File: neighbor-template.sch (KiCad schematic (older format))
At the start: 12 parts, among them J1 NEIGHBOR1, J2 NEIGHBOR2, J7 BONUS_ROW

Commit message: copy gsg-kicad-lib footprints to local library remove gsg-kicad-lib dependency
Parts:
- J1, J2: footprint gsg-modules:HEADER-2x20 -> neighbor:HEADER-2x20
- J7: footprint gsg-modules:HEADER-1x20 -> neighbor:HEADER-1x20
- MH1, MH2, MH3, MH4: footprint gsg-modules:HOLE126MIL-COPPER -> neighbor:HOLE126MIL-COPPER
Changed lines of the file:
@@
 LIBS:power
 LIBS:74xx
-LIBS:gsg-symbols
 LIBS:neighbor-template-cache
 EELAYER 29 0
@@
 F 0 "J2" H 15750 3900 50  0000 C CNN
 F 1 "NEIGHBOR2" V 15750 2850 50  0000 C CNN
-F 2 "gsg-modules:HEADER-2x20" H 15700 1900 60  0001 C CNN
+F 2 "neighbor:HEADER-2x20" H 15700 1900 60  0001 C CNN
 F 3 "" H 15700 1900 60  0000 C CNN
 F 4 "Samtec" H 15700 2850 60  0001 C CNN "Manufacturer"
@@
 F 0 "J1" H 15750 6250 50  0000 C CNN
 F 1 "NEIGHBOR1" V 15750 5200 50  0000 C CNN
-F 2 "gsg-modules:HEADER-2x20" H 15700 4250 60  0001 C CNN
+F 2 "neighbor:HEADER-2x20" H 15700 4250 60  0001 C CNN
 F 3 "" H 15700 4250 60  0000 C CNN
 F 4 "Samtec" H 15700 5200 60  0001 C CNN "Manufacturer"
@@
 F 0 "J7" H 15150 8050 50  0000 C CNN
 F 1 "BONUS_ROW" V 15250 7000 50  0000 C CNN
-F 2 "gsg-modules:HEADER-1x20" H 15150 7000 60  0001 C CNN
+F 2 "neighbor:HEADER-1x20" H 15150 7000 60  0001 C CNN
 F 3 "" H 15150 7000 60  0000 C CNN
 F 4 "Samtec" H 15150 7000 60  0001 C CNN "Manufacturer"
@@
 F 0 "MH3" H 13600 950 50  0000 C CNN
 F 1 "MOUNTING_HOLE" V 13750 850 50  0000 C CNN
-F 2 "gsg-modules:HOLE126MIL-COPPER" H 13650 850 60  0001 C CNN
+F 2 "neighbor:HOLE126MIL-COPPER" H 13650 850 60  0001 C CNN
 F 3 "" H 13650 850 60  0000 C CNN
 F 4 "DNP" H 13650 850 60  0001 C CNN "Note"
@@
 F 0 "MH4" H 14100 1100 50  0000 C CNN
 F 1 "MOUNTING_HOLE" V 14250 1000 50  0000 C CNN
-F 2 "gsg-modules:HOLE126MIL-COPPER" H 14150 1000 60  0001 C CNN
+F 2 "neighbor:HOLE126MIL-COPPER" H 14150 1000 60  0001 C CNN
 F 3 "" H 14150 1000 60  0000 C CNN
 F 4 "DNP" H 14150 1000 60  0001 C CNN "Note"
@@
 F 0 "MH1" H 12600 950 50  0000 C CNN
 F 1 "MOUNTING_HOLE" V 12750 850 50  0000 C CNN
-F 2 "gsg-modules:HOLE126MIL-COPPER" H 12650 850 60  0001 C CNN
+F 2 "neighbor:HOLE126MIL-COPPER" H 12650 850 60  0001 C CNN
 F 3 "" H 12650 850 60  0000 C CNN
 F 4 "DNP" H 12650 850 60  0001 C CNN "Note"
@@
 F 0 "MH2" H 13100 1100 50  0000 C CNN
 F 1 "MOUNTING_HOLE" V 13250 1000 50  0000 C CNN
-F 2 "gsg-modules:HOLE126MIL-COPPER" H 13150 1000 60  0001 C CNN
+F 2 "neighbor:HOLE126MIL-COPPER" H 13150 1000 60  0001 C CNN
 F 3 "" H 13150 1000 60  0000 C CNN
 F 4 "DNP" H 13150 1000 60  0001 C CNN "Note"

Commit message: change recommended alternate pin header parts fixes #1
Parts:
- J1, J2: Note Alternate: https://www.adafruit.com/products/2223 -> Alternate: SSQ-120-x3-x-D
- J7: Note (none) -> Alternate: SSQ-120-x3-x-S
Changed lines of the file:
@@
 EESchema Schematic File Version 4
-LIBS:power
-LIBS:74xx
 LIBS:neighbor-template-cache
-EELAYER 29 0
+EELAYER 30 0
 EELAYER END
 $Descr USLedger 17000 11000
@@
 F 5 "SSQ-120-23-G-D" H 15700 2850 60  0001 C CNN "Part Number"
 F 6 "CONN RCPT .100\" 40POS DUAL-ROW STACKING GOLD" H 15700 2850 60  0001 C CNN "Description"
-F 7 "Alternate: https://www.adafruit.com/products/2223" H 15700 2850 60  0001 C CNN "Note"
+F 7 "Alternate: SSQ-120-x3-x-D" H 15700 2850 60  0001 C CNN "Note"
 	1    15700 2850
 	1    0    0    -1
@@
 F 5 "SSQ-120-23-G-D" H 15700 5200 60  0001 C CNN "Part Number"
 F 6 "CONN RCPT .100\" 40POS DUAL-ROW STACKING GOLD" H 15700 5200 60  0001 C CNN "Description"
-F 7 "Alternate: https://www.adafruit.com/products/2223" H 15700 5200 60  0001 C CNN "Note"
+F 7 "Alternate: SSQ-120-x3-x-D" H 15700 5200 60  0001 C CNN "Note"
 	1    15700 5200
 	1    0    0    -1
@@
 F 5 "SSQ-120-23-G-S" H 15150 7000 60  0001 C CNN "Part Number"
 F 6 "CONN RCPT .100\" 20POS SINGLE-ROW STACKING GOLD" H 15150 7000 60  0001 C CNN "Description"
+F 7 "Alternate: SSQ-120-x3-x-S" H 15150 7000 50  0001 C CNN "Note"
 	1    15150 7000
 	0    -1   -1   0

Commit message: add links to How to Design a Neighbor closes #2
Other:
- note added: "How to Design a Neighbor:\nhttps://github.com/greatscottgadgets/greatfet/wiki/How-to-Design-a-Neighbor"
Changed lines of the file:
@@
 Wire Wire Line
 	3000 2250 3000 2200
+Text Notes 4900 950  0    100  ~ 0
+How to Design a Neighbor:\nhttps://github.com/greatscottgadgets/greatfet/wiki/How-to-Design-a-Neighbor
 $EndSCHEMATC

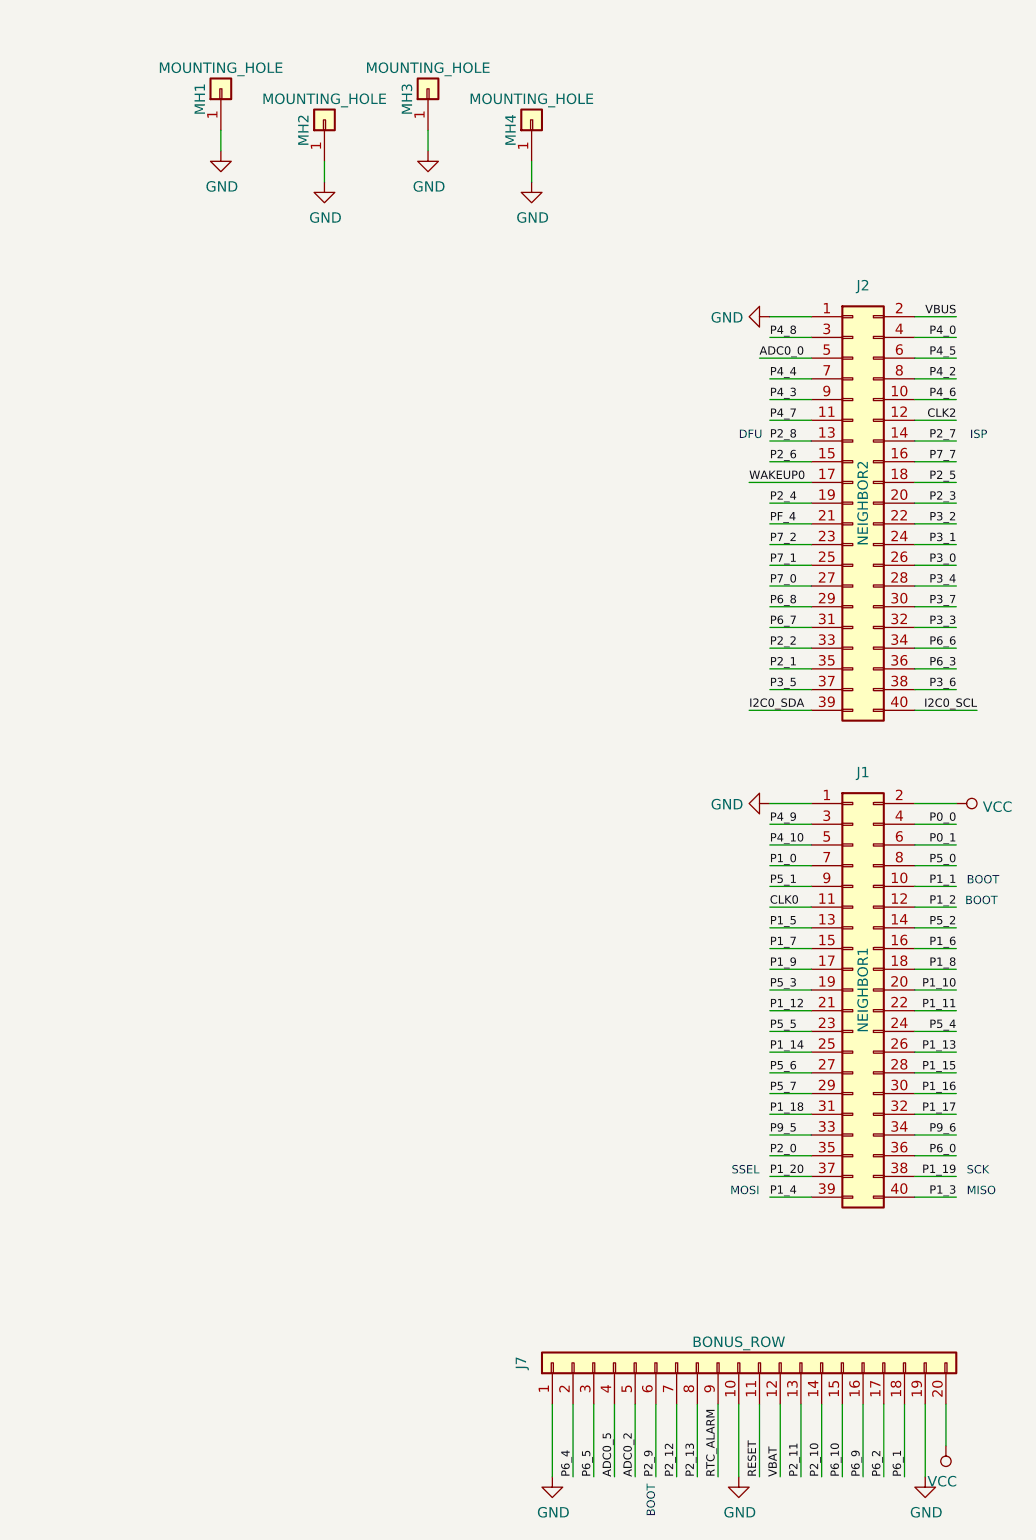
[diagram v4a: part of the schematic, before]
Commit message: add no-connect flags to SPIFI and boot pins closes #4
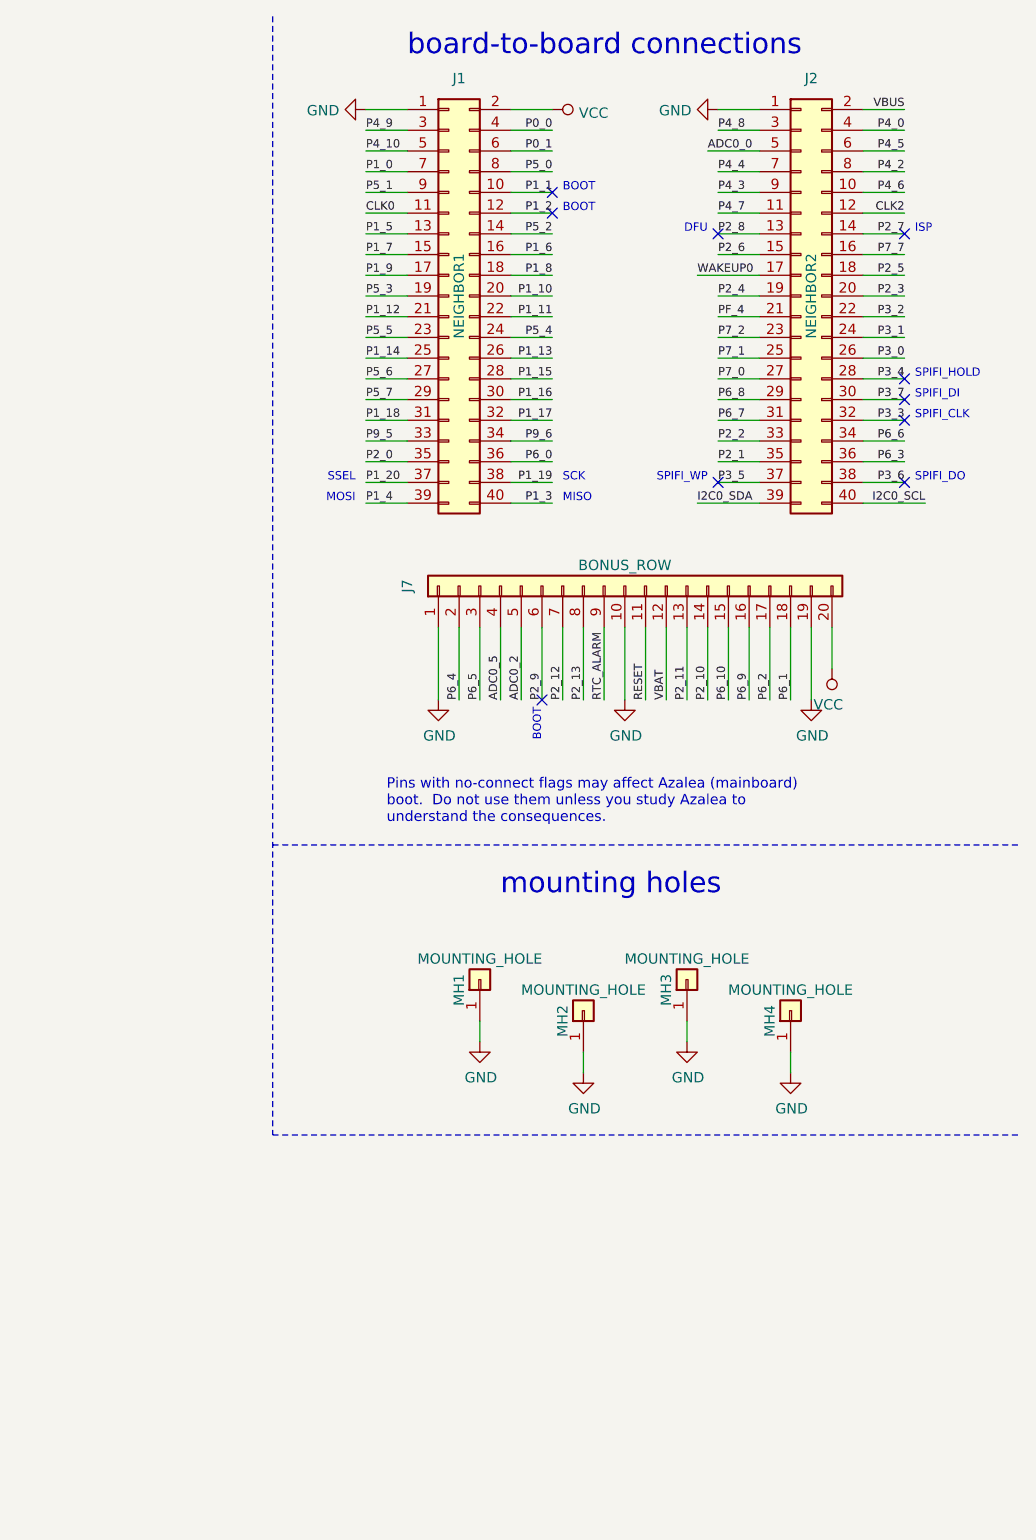
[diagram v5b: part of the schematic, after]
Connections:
- no-connect marks 0 -> 10
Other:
- note added: "Pins with no-connect flags may affect Azalea (mainboard)\nboot. Do not use them unless you study Azalea to\nunderstand the consequences."
- note added: "SPIFI_CLK"
- note added: "SPIFI_DI"
- note added: "SPIFI_DO"
- note added: "SPIFI_HOLD"
- note added: "SPIFI_WP"
- note added: "board-to-board connections"
- note added: "mounting holes"
- moved on the sheet: J1, J2, J7, MH1, MH2, MH3, MH4

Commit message: add identification EEPROM to layout
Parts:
- removed JP?: Jumper_3_Bridged12, symbol Jumper:Jumper_3_Bridged12
- added C1: 100nF, Capacitor_SMD:C_0603_1608Metric_Pad1.05x0.95mm_HandSolder, symbol Device:C
- added JP2: Jumper_3_Bridged12, neighbor:0603-JUMPER-3-BRIDGED12, symbol Jumper:Jumper_3_Bridged12
- JP1, JP3: renamed from JP?; footprint (none) -> neighbor:0603-JUMPER-3-BRIDGED12
- R1: renamed from R?; footprint (none) -> Resistor_SMD:R_0603_1608Metric_Pad1.05x0.95mm_HandSolder
- gave numbers to parts that had none: 1
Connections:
- net GND: now also C1.1, JP2.1 (A)
- net VCC: now also C1.2, JP2.3 (B)
- net E0: now reaches JP1.2 (C), U1.1 (E0)
- net E1: now reaches U1.2 (E1)
- net E1: now also JP2.2 (C)
- net E2: now reaches JP3.2 (C), U1.3 (E2)
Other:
- note added: "J7 is optional"
- note added: "WC is by default pulled up, enabling write protection.\nTo disable write protection temporarily, configure P2_1\n(J2_P35) as GPIO and output low. To disable write\nprotection permanently, remove R1."
- note added: "neighbor identification EEPROM (optional)"
- note removed: "WC is by default pulled up, and the write protection is locked.\nTo enable write configuration ... FIXME"
- moved on the sheet: JP1, JP3, R1, U1

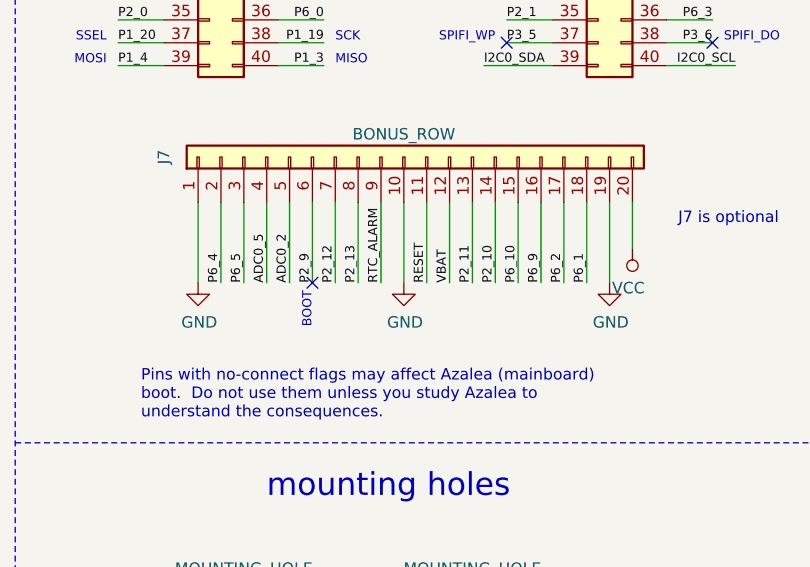
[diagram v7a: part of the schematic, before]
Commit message: change J7_P10 from GND to RTCX1 fixes #7
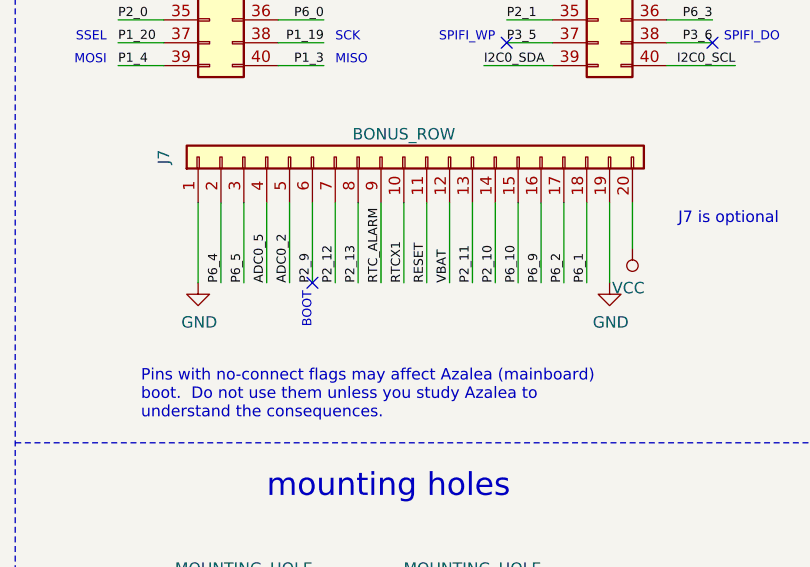
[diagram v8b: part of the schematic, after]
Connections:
- net GND: no longer J7.10 (Pin_10)
- new net RTCX1: J7.10 (Pin_10)
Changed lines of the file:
@@
-$EndComp
-$Comp
-L power:GND #PWR0104
-U 1 1 5CCC4966
-P 14600 3800
-F 0 "#PWR0104" H 14600 3550 50  0001 C CNN
-F 1 "GND" H 14605 3627 50  0000 C CNN
-F 2 "" H 14600 3800 50  0001 C CNN
-F 3 "" H 14600 3800 50  0001 C CNN
-	1    14600 3800
-	1    0    0    -1
 $EndComp
 $Comp
@@
 Text Label 14600 8050 2    40   ~ 0
 E2
+Text Label 14600 3800 1    40   ~ 0
+RTCX1
 $EndSCHEMATC
